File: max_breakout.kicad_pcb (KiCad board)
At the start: 4 copper layers, 50.8 x 25.4 mm, 50 parts, among them J1 USB_B_Micro, J2 Left, J3 Right, J4 JTAG, SW1 User, U1 74HCT125, U2 LP2985-3.3, U3 LP2985-5.0, U4 TPS2113A, U5 EPM7064STC44, X1 CTX-636 50mhz

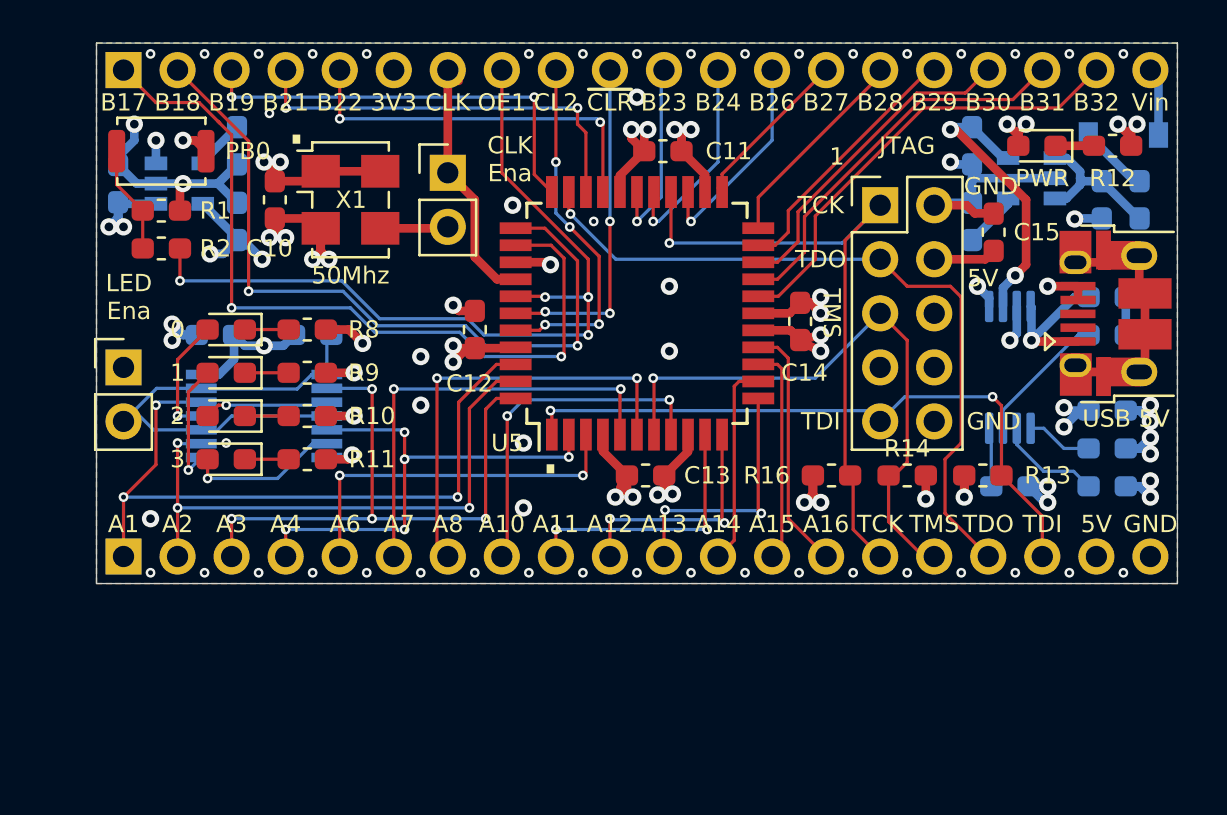
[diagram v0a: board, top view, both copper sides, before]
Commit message: Added pmod
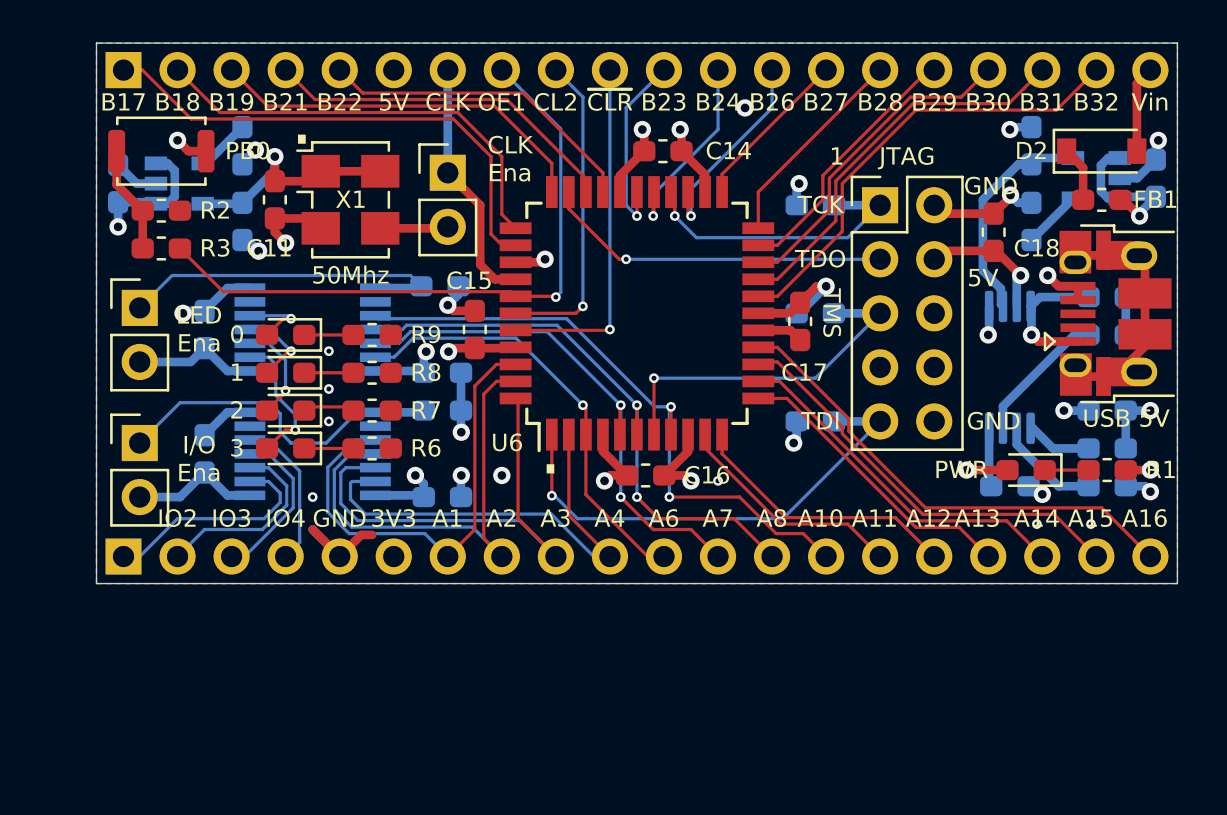
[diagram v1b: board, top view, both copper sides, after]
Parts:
- removed the C1 at (130.0, 105.2)
- removed the R5 at (134.6, 105.2)
- removed the U1 at (132.3, 109.0)
- added C13: 100nF, Capacitor_SMD:C_0603_1608Metric_Pad1.05x0.95mm_HandSolder, B.Cu at (140.7, 112.8)
- added C15: 100nF, Capacitor_SMD:C_0603_1608Metric_Pad1.05x0.95mm_HandSolder, F.Cu at (142.2, 104.9)
- added C4: 100nF, Capacitor_SMD:C_0603_1608Metric_Pad1.05x0.95mm_HandSolder, B.Cu at (129.5, 104.9)
- added C7: 100nF, Capacitor_SMD:C_0603_1608Metric_Pad1.05x0.95mm_HandSolder, B.Cu at (140.7, 106.9)
- added JP2: ena, Connector_PinHeader_2.54mm:PinHeader_1x02_P2.54mm_Vertical, F.Cu at (126.5, 110.2)
- added R13: 1K, Resistor_SMD:R_0603_1608Metric_Pad1.05x0.95mm_HandSolder, B.Cu at (140.7, 108.7)
- added R4: 1K, Resistor_SMD:R_0603_1608Metric_Pad1.05x0.95mm_HandSolder, B.Cu at (140.6, 102.9)
- added U4: TXB0104PW, Package_SO:TSSOP-14_4.4x5mm_P0.65mm, B.Cu at (134.6, 104.9)
- added U5: TXB0104PW, Package_SO:TSSOP-14_4.4x5mm_P0.65mm, B.Cu at (134.6, 110.7)
- C12, R16: moved to B.Cu
- D2: renamed from D1; moved to F.Cu
- FB1: moved to F.Cu
- R14: renamed from R13; moved to B.Cu
- R15: renamed from R14; moved to B.Cu
- moved D1 15.2 mm to (168.1, 111.5)
- moved R1 15.2 mm to (172.0, 111.5)
- moved C12 14.0 mm to (129.5, 110.7)
- moved R16 12.7 mm to (158.2, 99.1)
- moved R15 8.76 mm to (158.2, 104.1), turned to 0 degrees
- moved R14 8.27 mm to (158.2, 109.2)
- moved R9 6.59 mm to (137.4, 105.2)
- moved R6 6.37 mm to (137.4, 110.5)
- moved R8 3.66 mm to (137.4, 106.9)
- moved R7 3.53 mm to (137.4, 108.7)
- moved U2 3.05 mm to (171.4, 97.8)
- moved JP1 2.90 mm to (126.5, 103.9)
- moved D3 2.84 mm to (133.3, 110.5)
- moved D6 2.81 mm to (133.3, 105.2)
- moved D4 2.81 mm to (133.3, 108.7)
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- renumbered C2 to C1, C8 to C10, C10 to C11, C11 to C14, C13 to C16, C14 to C17, C15 to C18, C3 to C2, C4 to C3, C9 to C8, C7 to C9, D6 to D1, D5 to D3, D3 to D5, D2 to D6, JP2 to JP3, R12 to R1, R4 to R10, R6 to R11, R7 to R12, R1 to R2, R2 to R3, R3 to R5, R8 to R6, R9 to R7, R10 to R8, R11 to R9, U2 to U1, U3 to U2, U4 to U3, U5 to U6
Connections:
- net 5V renamed 5Vin
- C12 pad 1: +5V -> +3V3
- D3 pad 1: Net-(D5-Pad1) -> Net-(D3-Pad1)
- D5 pad 1: Net-(D3-Pad1) -> Net-(D5-Pad1)
- D6 pad 1: Net-(D2-Pad1) (its old number) -> Net-(D6-Pad1)
- J2 pad 1: /A1 -> /PMOD1
- J2 pad 10: /A12 -> /A5
- J2 pad 11: /A13 -> /A6
- J2 pad 12: /A14 -> /A7
- J2 pad 13: /A15 -> /A8
- J2 pad 14: /A16 -> /A10
- J2 pad 15: /TCK -> /A11
- J2 pad 16: /TMS -> /A12
- J2 pad 17: /TDO -> /A13
- J2 pad 18: /TDI -> /A14
- J2 pad 19: +5V -> /A15
- J2 pad 2: /A2 -> /PMOD2
- J2 pad 20: GND -> /A16
- J2 pad 3: /A3 -> /PMOD3
- J2 pad 4: /A4 -> /PMOD4
- J2 pad 5: /A6 -> GND
- J2 pad 6: /A7 -> +3V3
- J2 pad 7: /A8 -> /A1
- J2 pad 8: /A10 -> /A2
- J2 pad 9: /A11 -> /A3
- J3 pad 10: /GCLRn -> /CLK2
- J3 pad 6: +3V3 -> +5V
- J3 pad 9: /CLK2 -> /GCLRn
- JP1 pad 1: GND -> Net-(JP1-Pad1)
- JP1 pad 2: /ENA -> +3V3
- R6 pad 2: Net-(D2-Pad1) (its old number) -> Net-(D3-Pad1)
- R7 pad 2: Net-(D3-Pad1) -> Net-(D4-Pad1)
- R8 pad 2: Net-(D4-Pad1) -> Net-(D5-Pad1)
- R9 pad 2: Net-(D5-Pad1) -> Net-(D6-Pad1)
- U6 pad 2: /A4 -> /A5
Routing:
- net /A4: track 24.0 -> 0.00 mm, vias 5 -> 0
- net /ENA: track 22.2 -> 0.00 mm
- net /A5: track 0.00 -> 21.8 mm
- net GND: track 77.0 -> 56.6 mm, vias 82 -> 29
- net /TDO: track 35.5 -> 16.4 mm
- net /TCK: track 31.5 -> 14.1 mm
- net Net-(JP1-Pad1): track 0.00 -> 16.3 mm
- net Net-(JP2-Pad1): track 0.00 -> 16.1 mm
- net /B18: track 35.8 -> 20.6 mm, vias 2 -> 0
- net /B17: track 38.2 -> 24.0 mm, vias 2 -> 0
- net /A10: track 16.3 -> 29.8 mm
- net +3V3: track 12.7 -> 24.6 mm, vias 4 -> 1
- net /TMS: track 28.4 -> 16.7 mm
- net /A1: track 33.5 -> 22.3 mm, vias 3 -> 0
- net /A16: track 12.3 -> 22.8 mm
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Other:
- board text added: "I/O Ena"
- board text added: "IO2"
- board text added: "IO3"
- board text added: "IO4"
- board text added: "MAX7000S Breakout Board v3.5"
- board text added: "by Hyiger Designs"
- board text removed: "MAX7000S Breakout Board v3.2 by Hyiger Designs"

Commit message: Reorganized pins
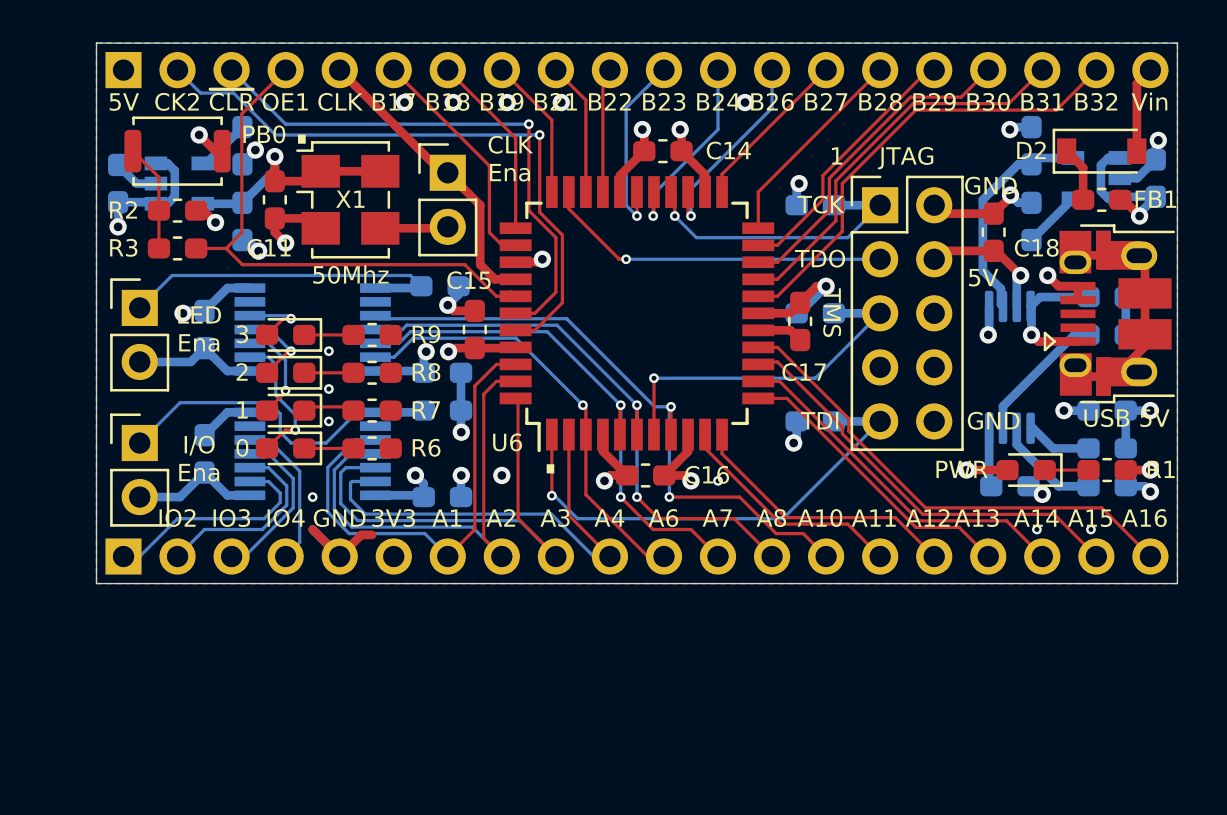
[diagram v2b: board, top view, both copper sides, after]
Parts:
- moved R2 0.76 mm to (128.3, 99.3)
- moved R3 0.76 mm to (128.3, 101.1)
- moved SW1 0.76 mm to (128.3, 96.5)
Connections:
- J3 pad 1: /B17 -> +5V
- J3 pad 10: /CLK2 -> /B22
- J3 pad 2: /B18 -> /CLK2
- J3 pad 3: /B19 -> /GCLRn
- J3 pad 4: /B21 -> /OE1
- J3 pad 5: /B22 -> /CLK
- J3 pad 6: +5V -> /B17
- J3 pad 7: /CLK -> /B18
- J3 pad 8: /OE1 -> /B19
- J3 pad 9: /GCLRn -> /B21
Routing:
- net /CLK2: track 16.6 -> 30.1 mm
- net /B18: track 20.6 -> 8.75 mm
- net /B19: track 18.2 -> 6.70 mm
- net /B17: track 24.0 -> 12.5 mm
- net /GCLRn: track 14.9 -> 25.7 mm
- net /B21: track 16.9 -> 6.95 mm
- net /B22: track 15.3 -> 5.87 mm
- net /OE1: track 30.5 -> 25.8 mm, vias 1 -> 0
- net /CLK: track 12.2 -> 14.5 mm
- net +5V: track 44.4 -> 42.7 mm
- net GND: track 56.6 -> 57.6 mm, vias 29 -> 34
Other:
- board text added: "CK2"
- board text removed: "CL2"

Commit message: added pmod connector
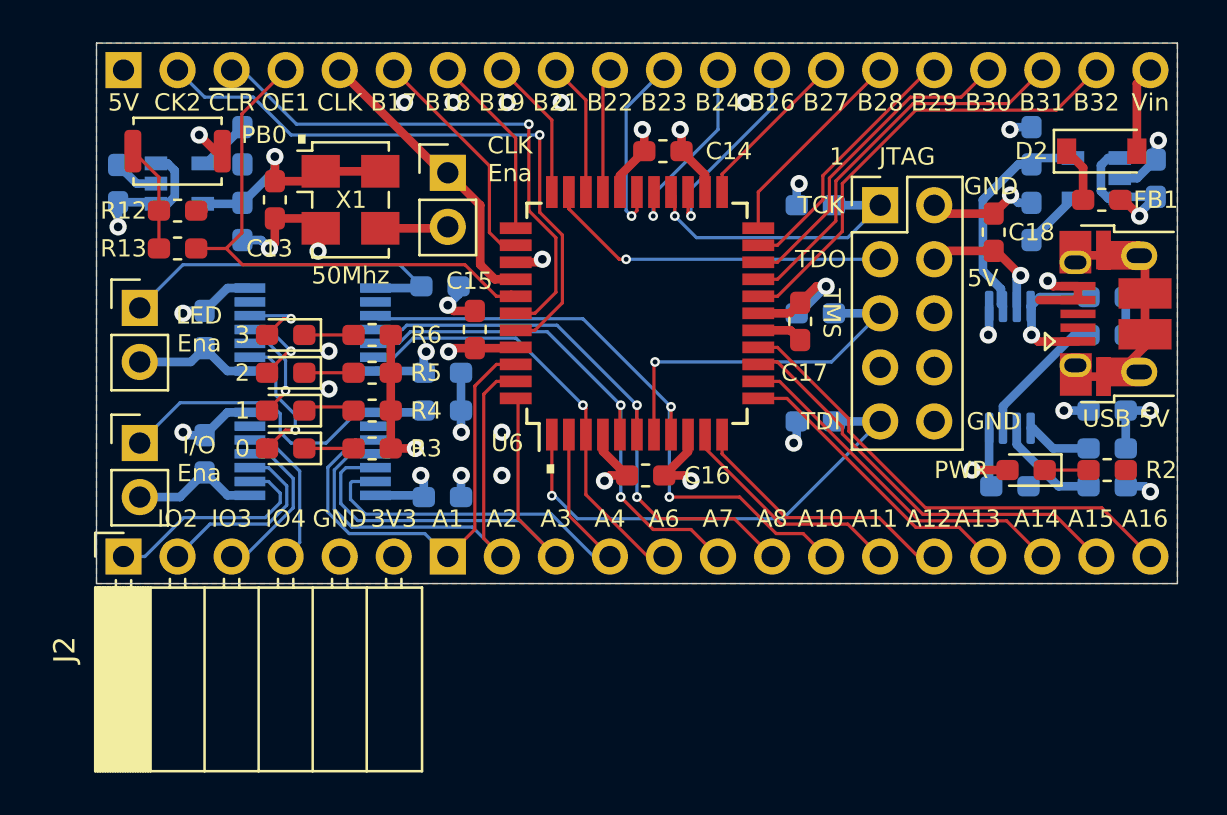
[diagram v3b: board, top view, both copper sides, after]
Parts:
- added J2: PMOD, Connector_PinSocket_2.54mm:PinSocket_1x06_P2.54mm_Horizontal, F.Cu at (125.7, 115.6)
- J3: renamed from J2; footprint Connector_PinHeader_2.54mm:PinHeader_1x20_P2.54mm_Vertical -> Connector_PinHeader_2.54mm:PinHeader_1x14_P2.54mm_Vertical
- moved J3 15.2 mm to (141.0, 115.6)
- renumbered C4 to C1, C12 to C11, C13 to C12, C11 to C13, C1 to C2, C2 to C3, C3 to C4, C7 to C5, C5 to C6, C6 to C7, J3 to J4, J4 to J5, R4 to R1, R11 to R10, R12 to R11, R2 to R12, R3 to R13, R1 to R2, R6 to R3, R7 to R4, R8 to R5, R9 to R6, R5 to R7, R10 to R8, R13 to R9, U4 to U1, U1 to U2, U2 to U3, U3 to U4
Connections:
- J3 pad 1: /PMOD1 -> /A1
- J3 pad 10: /A5 -> /A12
- J3 pad 11: /A6 -> /A13
- J3 pad 12: /A7 -> /A14
- J3 pad 13: /A8 -> /A15
- J3 pad 14: /A10 -> /A16
- J3 pad 2: /PMOD2 -> /A2
- J3 pad 3: /PMOD3 -> /A3
- J3 pad 4: /PMOD4 -> /A5
- J3 pad 5: GND -> /A6
- J3 pad 6: +3V3 -> /A7
- J3 pad 7: /A1 -> /A8
- J3 pad 8: /A2 -> /A10
- J3 pad 9: /A3 -> /A11
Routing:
- net GND: track 57.6 -> 60.0 mm, vias 34 -> 28
- net /B17: track 12.5 -> 11.0 mm
- net +3V3: track 24.6 -> 23.1 mm
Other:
- board text added: "EPM7064STC44 * To Program Use: Quartus II 13.0sp1 * Use RioRand USB Blaster"
- board text removed: "EPM7064STC44 * To Program Use: Quartus II 13.0sp1"

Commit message: removed leds, added full pmod
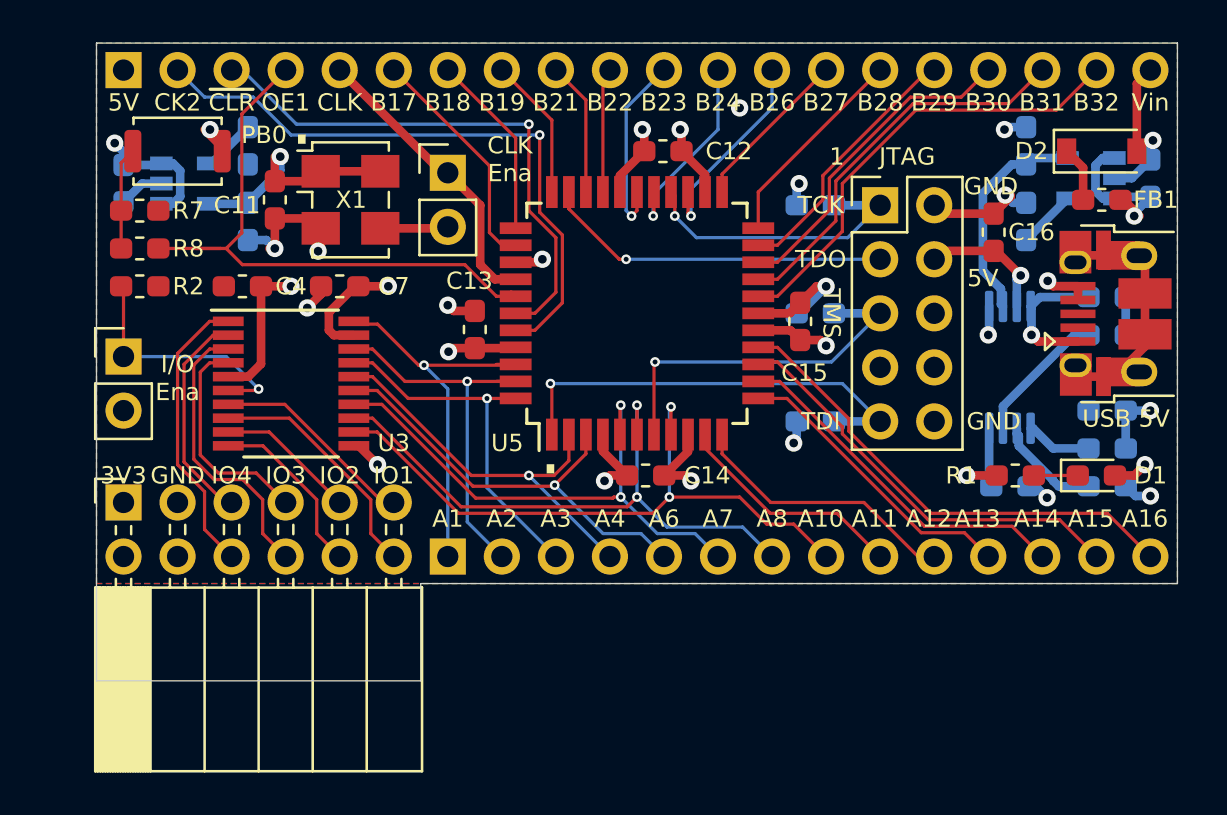
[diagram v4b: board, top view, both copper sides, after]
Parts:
- removed the C11 at (129.5, 110.7)
- removed the C12 at (140.7, 112.8)
- removed the C3 at (125.5, 98.0)
- removed the C6 at (131.3, 96.3)
- removed D3, D4, D5, D6: GRN, LED_SMD:LED_0603_1608Metric_Pad1.05x0.95mm_HandSolder
- removed the JP2 at (126.5, 110.2)
- removed the R3 at (137.4, 110.5)
- removed the R4 at (137.4, 108.7)
- removed the R5 at (137.4, 106.9)
- removed the R6 at (137.4, 105.2)
- removed the R9 at (140.7, 108.7)
- removed the U2 at (128.4, 98.0)
- removed the U5 at (134.6, 110.7)
- added C2: 1uF 35V, Capacitor_SMD:C_0603_1608Metric_Pad1.05x0.95mm_HandSolder, B.Cu at (125.7, 98.0)
- added C5: 10nF, Capacitor_SMD:C_0603_1608Metric_Pad1.05x0.95mm_HandSolder, B.Cu at (131.6, 96.3)
- added U3: TXB0108PWR, Package_SO:TSSOP-20_4.4x6.5mm_P0.65mm, F.Cu at (133.6, 107.4)
- C4: renamed from C1; moved to F.Cu
- C7: renamed from C5; moved to F.Cu
- J2: footprint Connector_PinSocket_2.54mm:PinSocket_1x06_P2.54mm_Horizontal -> max_breakout:PinSocket_2x06_Top_Bottom_P2.54mm_Horizontal
- R2: renamed from R1; moved to F.Cu
- U1: value TXB0104PW -> LP2985-3.3; footprint Package_SO:TSSOP-14_4.4x5mm_P0.65mm -> Package_TO_SOT_SMD:SOT-23-5
- moved R2 14.1 mm to (126.5, 102.9)
- moved U1 9.12 mm to (128.6, 98.0)
- moved C7 6.31 mm to (135.9, 102.9), turned to 180 degrees
- moved R1 4.33 mm to (167.6, 111.8), turned to 180 degrees
- moved D1 3.31 mm to (171.4, 111.8), turned to 0 degrees
- moved C4 2.70 mm to (131.3, 102.9), turned to 180 degrees
- moved J2 2.54 mm to (125.7, 113.0)
- moved JP1 2.41 mm to (125.7, 106.2)
- moved R7 1.78 mm to (126.5, 99.3)
- moved R8 1.78 mm to (126.5, 101.1)
- moved C10 0.25 mm to (168.1, 96.3)
- moved C3 0.25 mm to (174.0, 97.8)
- moved C6 0.25 mm to (168.1, 99.8)
- moved C9 0.25 mm to (131.6, 99.8)
- moved U2 0.25 mm to (171.2, 97.8)
- renumbered C2 to C1, C13 to C11, C14 to C12, C15 to C13, C16 to C14, C17 to C15, C18 to C16, C4 to C3, C7 to C6, JP3 to JP2, R2 to R1, R15 to R10, R16 to R11, R7 to R3, R8 to R4, R10 to R5, R11 to R6, R12 to R7, R13 to R8, R14 to R9, U3 to U2, U6 to U5
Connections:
- J2 pad 1: /PMOD1 -> +3V3
- J2 pad 2: /PMOD2 -> GND
- J2 pad 3: /PMOD3 -> /PMOD4
- J2 pad 4: /PMOD4 -> /PMOD3
- J2 pad 5: GND -> /PMOD2
- J2 pad 6: +3V3 -> /PMOD1
- U1 pad 1: +3V3 -> +5V
- U1 pad 2: Net-(D3-Pad2) -> GND
- U1 pad 3: Net-(D4-Pad2) -> +5V
- U1 pad 5: Net-(D6-Pad2) -> +3V3
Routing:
- net Net-(JP2-Pad1): track 16.1 -> 0.00 mm
- net GND: track 60.0 -> 44.6 mm, vias 28 -> 19
- net /PMOD8: track 0.00 -> 13.6 mm
- net /PMOD7: track 0.00 -> 13.5 mm
- net /PMOD5: track 0.00 -> 11.4 mm
- net /PMOD6: track 0.00 -> 8.33 mm
- net Net-(D3-Pad2): track 6.51 -> 0.00 mm, vias 1 -> 0
- net /A3: track 22.5 -> 17.2 mm, vias 0 -> 1
- net +3V3: track 23.1 -> 18.0 mm, vias 1 -> 2
- net Net-(JP1-Pad1): track 16.7 -> 11.8 mm, vias 0 -> 1
- net Net-(D4-Pad2): track 4.73 -> 0.00 mm, vias 1 -> 0
- net /A2: track 22.6 -> 18.0 mm, vias 0 -> 1
- net Net-(D6-Pad2): track 3.44 -> 0.00 mm, vias 1 -> 0
- net /A1: track 22.3 -> 18.8 mm, vias 0 -> 1
- net /PMOD4: track 7.23 -> 10.5 mm
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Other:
- board size 50.8 x 25.4 mm -> 50.8 x 30 mm
- board text added: "IO1"
- board text removed: "0"
- board text removed: "2"
- board text removed: "3"
- board text removed: "50Mhz"
- board text removed: "LED Ena"
- board text removed: "PWR"

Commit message: replaced level translator with push-pull version
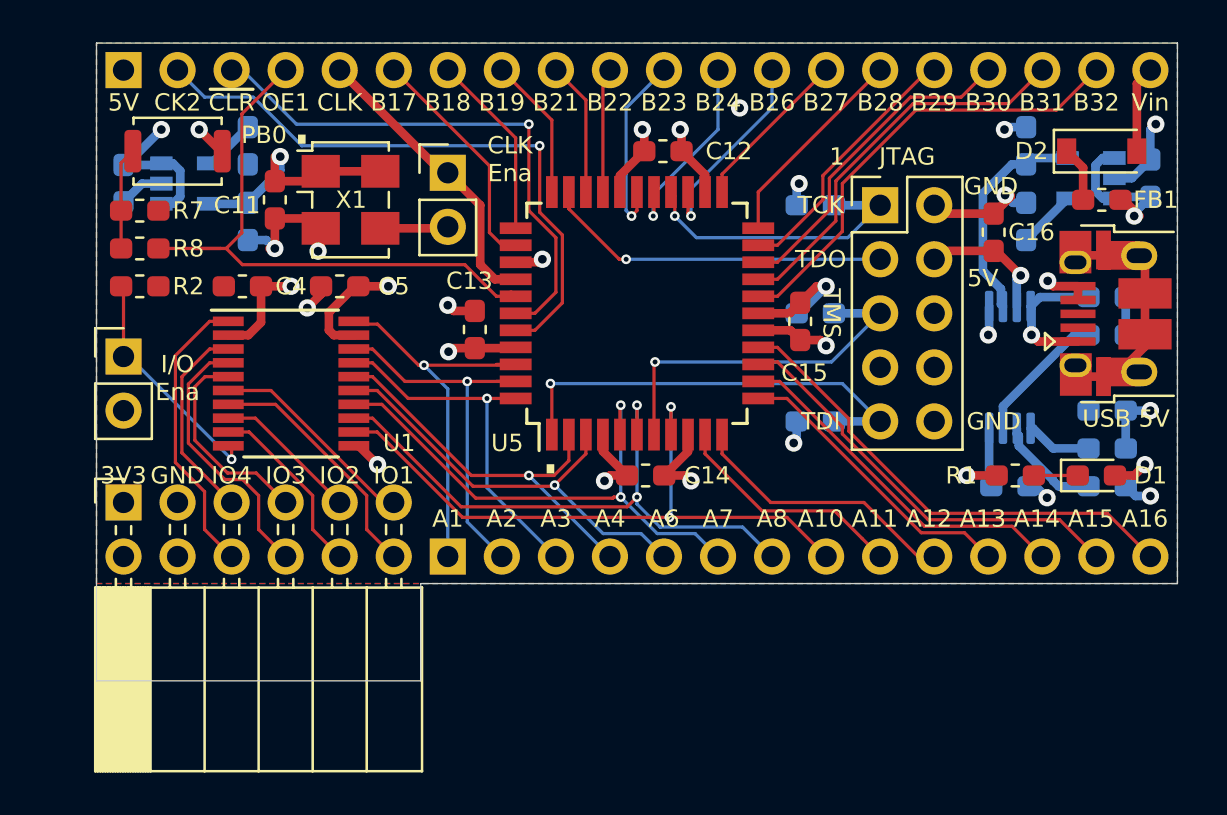
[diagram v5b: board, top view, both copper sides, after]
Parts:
- removed the U3 at (133.6, 107.4)
- added U1: TXS0108EPW, Package_SO:TSSOP-20_4.4x6.5mm_P0.65mm, F.Cu at (133.6, 107.4)
- R2: value 1K -> 100K
- renumbered C7 to C5, C5 to C6, C6 to C7, U1 to U2, U2 to U3
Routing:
- net +3V3: track 18.0 -> 16.1 mm
- net +5V: track 41.8 -> 43.4 mm
- net /PMOD4: track 10.5 -> 9.60 mm
- net GND: track 44.6 -> 45.5 mm
- net /PMOD7: track 13.5 -> 12.8 mm
- net Net-(JP1-Pad1): track 11.8 -> 11.1 mm
- net /PMOD3: track 10.3 -> 9.76 mm
